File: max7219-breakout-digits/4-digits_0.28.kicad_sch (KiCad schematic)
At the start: 5 parts, among them J1 Conn_02x08_Odd_Even, U1 HDSM-443B_CC_2Digit_7Segment_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, U2 HDSM-443B_CC_2Digit_7Segment_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

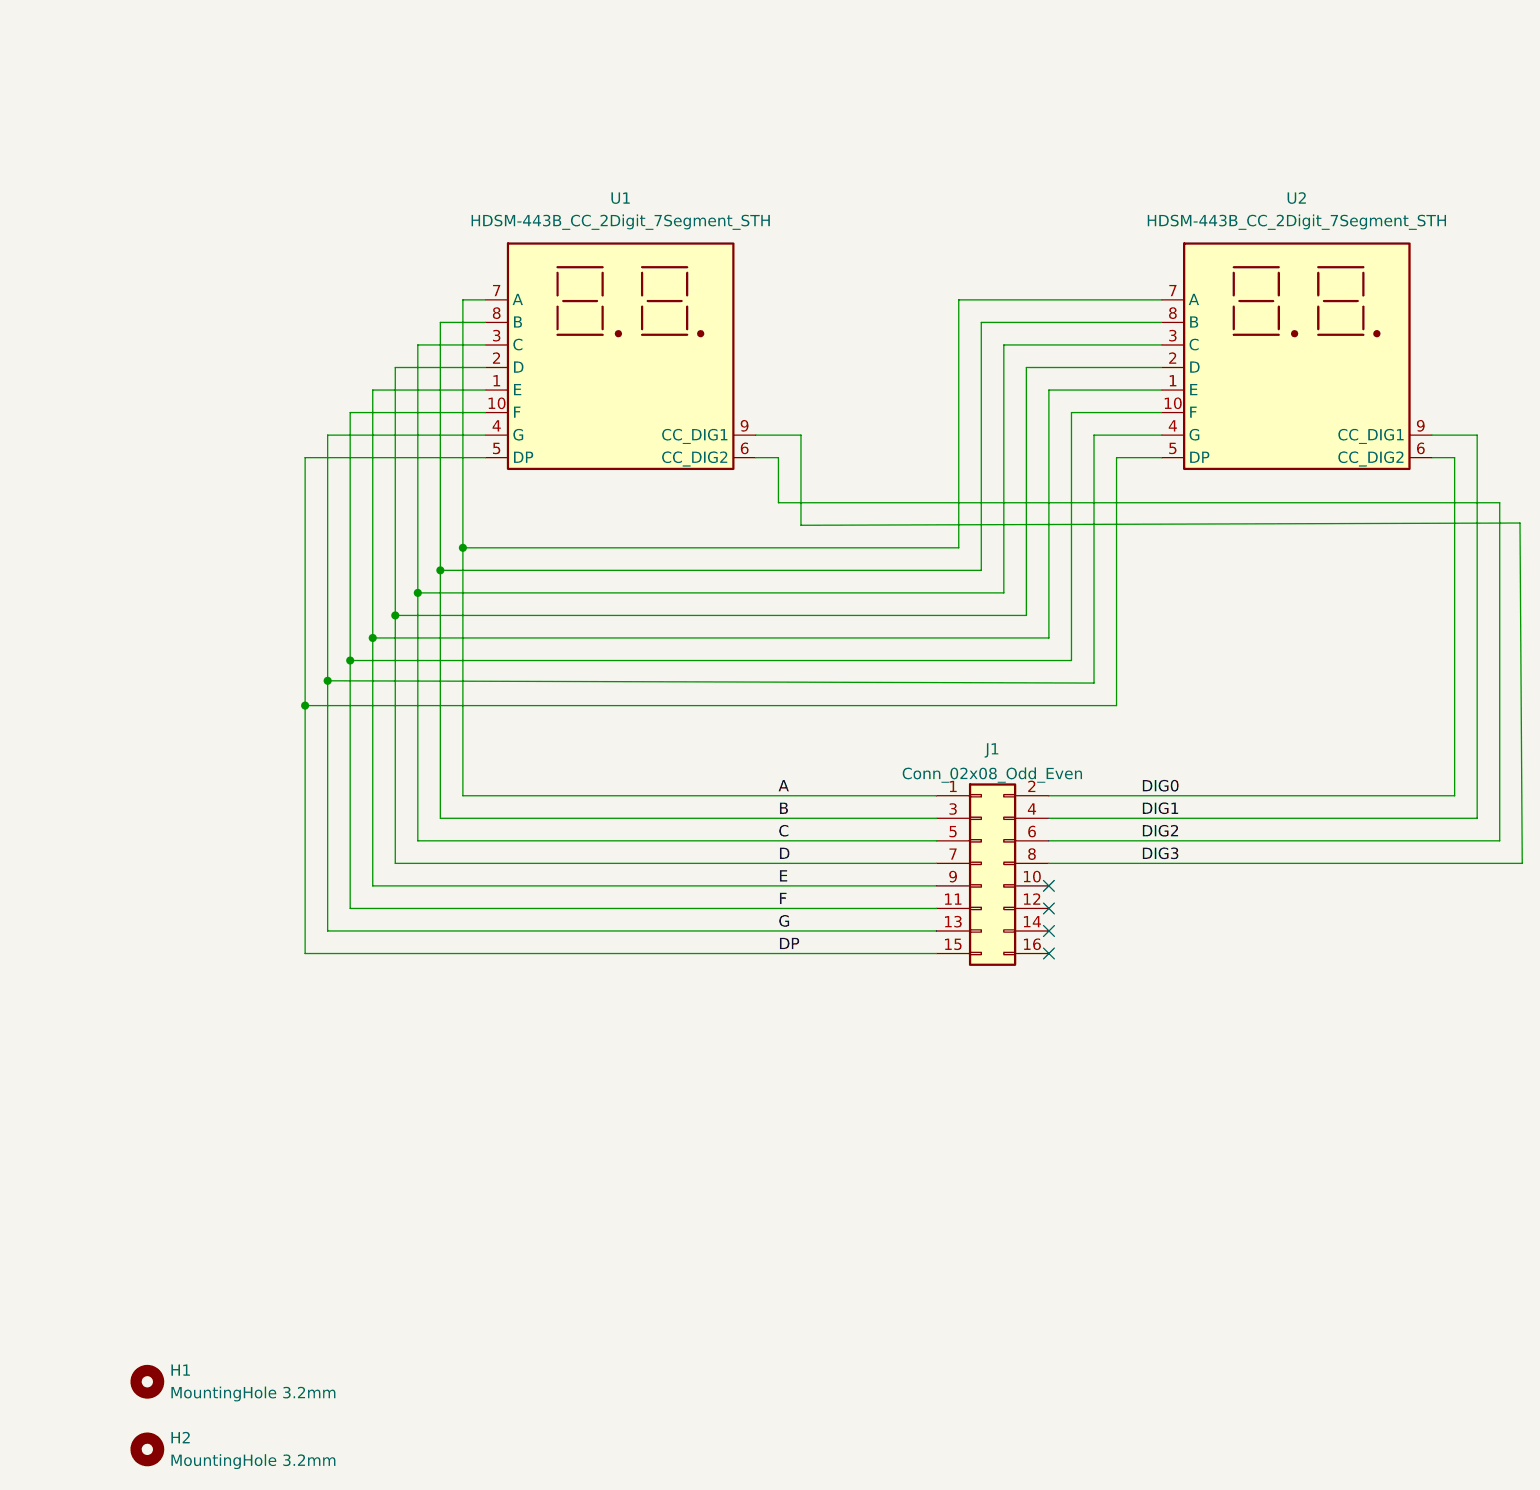
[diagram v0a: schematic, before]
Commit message: rotate IDC on 0.28 displays, plated mounting holes for 0.35 displays, set version for 0.35 displays
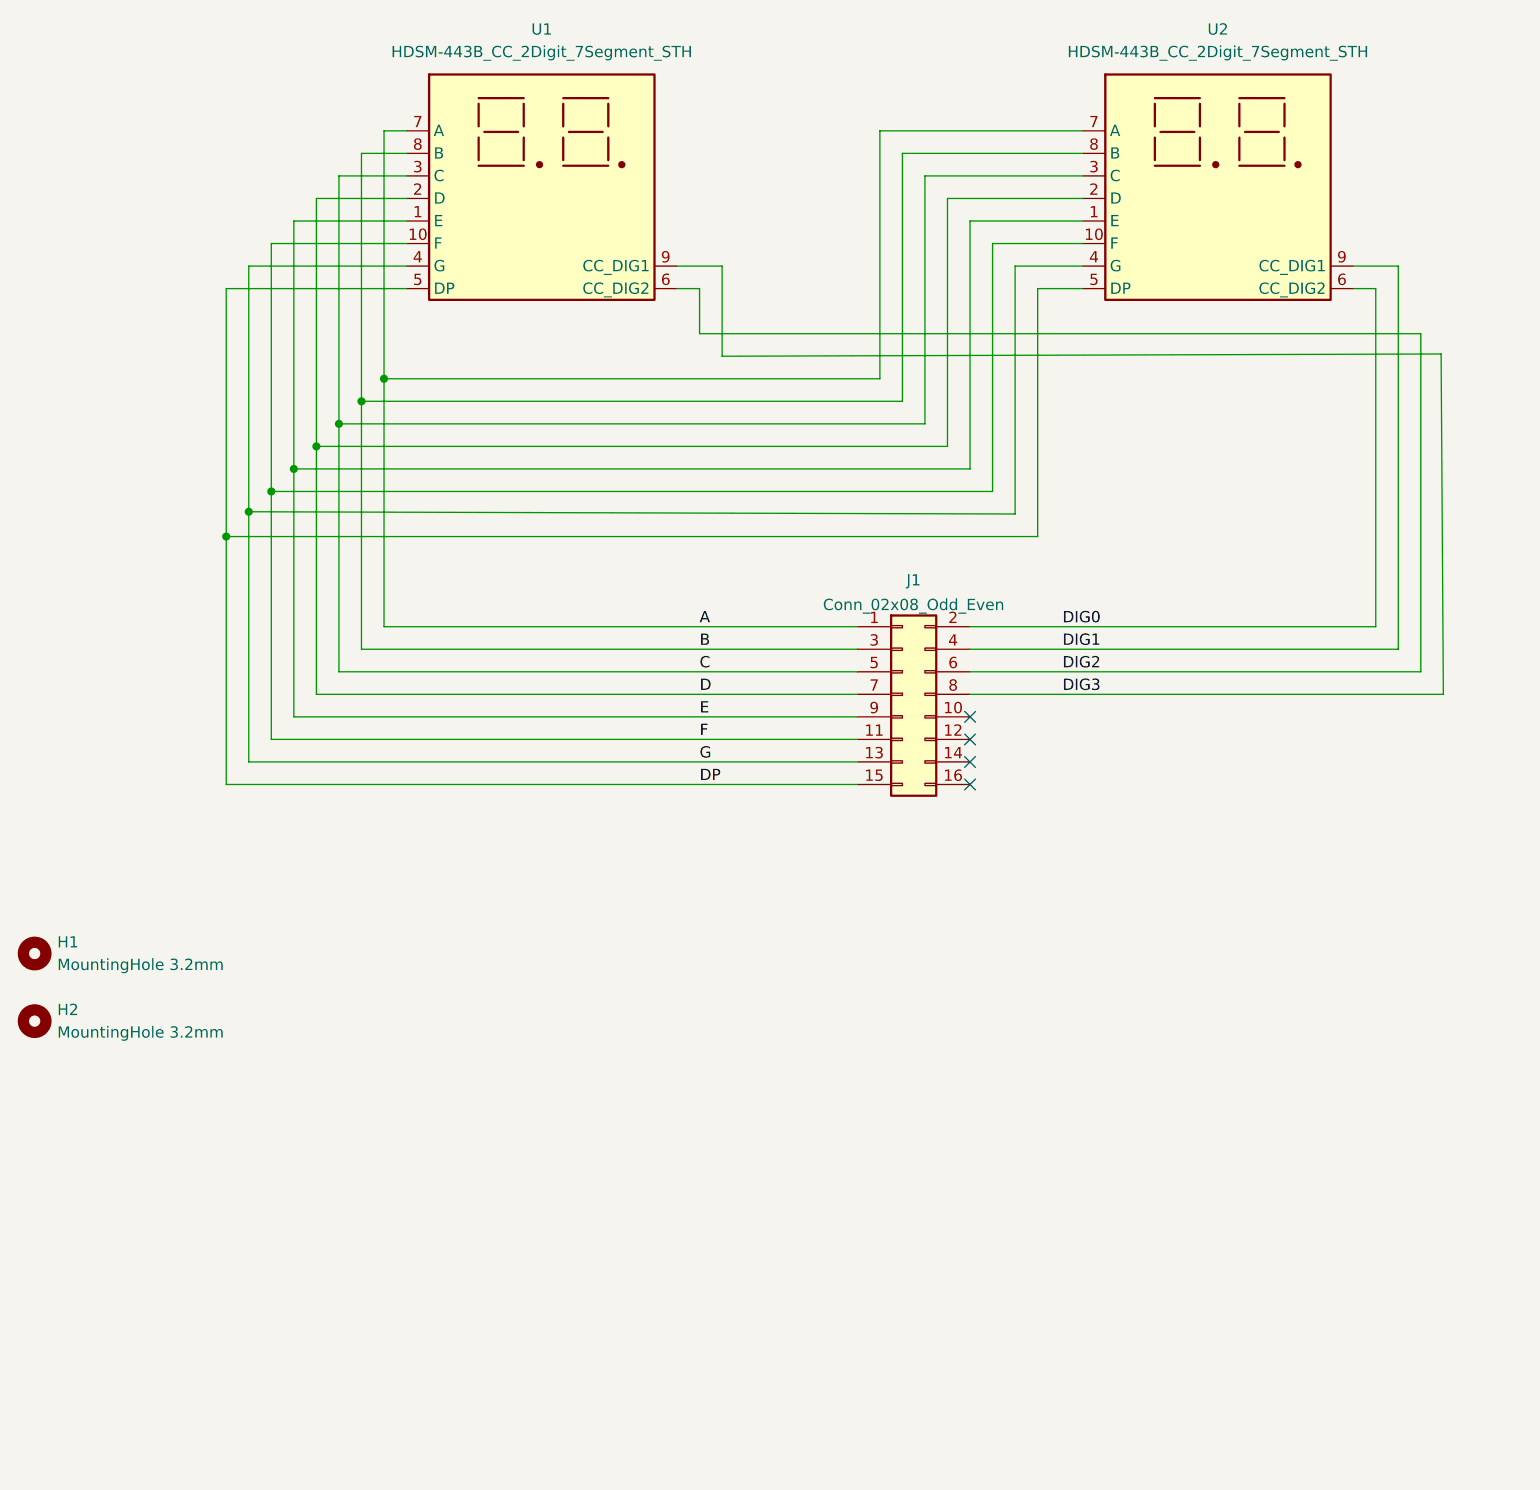
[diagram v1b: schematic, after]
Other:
- moved on the sheet: H1, H2, J1, U1, U2
